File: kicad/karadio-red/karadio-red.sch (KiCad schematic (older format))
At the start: 18 parts, among them J1 CTRL, J2 PWR, J3 UART, J4 FW, J5 VS1053_RED, SW1 RESET, U1 AMS1117-3.3, U2 ESP-12E

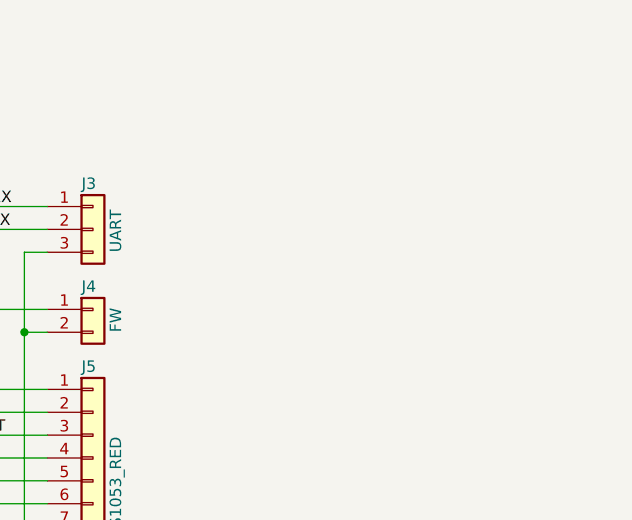
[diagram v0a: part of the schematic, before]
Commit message: Add optional RAM to karadio project
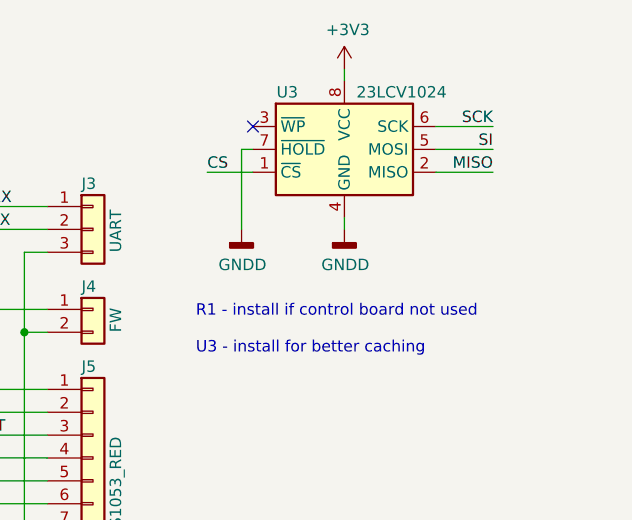
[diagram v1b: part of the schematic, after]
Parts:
- added U3: 23LCV1024, Package_SO:SO-8_3.9x4.9mm_P1.27mm, symbol Memory_EEPROM:25LCxxx
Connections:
- net +3V3: now also U3.8 (VCC)
- net CS: now also U3.1 (~CS)
- net GNDD: now also U3.4 (GND), U3.7 (~HOLD)
- net MISO: now also U3.2 (MISO)
- net SCK: now also U3.6 (SCK)
- net SI: now also U3.5 (MOSI)
- no-connect marks 6 -> 7
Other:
- note added: "R1 - install if control board not used\n\nU3 - install for better caching"
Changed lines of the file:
@@
 EESchema Schematic File Version 4
+LIBS:karadio-red-cache
 EELAYER 29 0
 EELAYER END
@@
 Text Label 4850 3300 0    50   ~ 0
 ~RST
+$Comp
+L Memory_EEPROM:25LCxxx U3
+U 1 1 5D361D11
+P 9000 3050
+F 0 "U3" H 8750 3300 50  0000 C CNN
+F 1 "23LCV1024" H 9250 3300 50  0000 C CNN
+F 2 "Package_SO:SO-8_3.9x4.9mm_P1.27mm" H 9000 3050 50  0001 C CNN
+F 3 "http://ww1.microchip.com/downloads/en/DeviceDoc/21832H.pdf" H 9000 3050 50  0001 C CNN
+	1    9000 3050
+	1    0    0    -1
+$EndComp
+$Comp
+L power:+3V3 #PWR0120
+U 1 1 5D3667F3
+P 9000 2700
+F 0 "#PWR0120" H 9000 2550 50  0001 C CNN
+F 1 "+3V3" H 9015 2873 50  0000 C CNN
+F 2 "" H 9000 2700 50  0001 C CNN
+F 3 "" H 9000 2700 50  0001 C CNN
+	1    9000 2700
+	1    0    0    -1
+$EndComp
+Wire Wire Line
+	9000 2700 9000 2750
+$Comp
+L power:GNDD #PWR0121
+U 1 1 5D369461
+P 9000 3400
+F 0 "#PWR0121" H 9000 3150 50  0001 C CNN
+F 1 "GNDD" H 9004 3245 50  0000 C CNN
+F 2 "" H 9000 3400 50  0001 C CNN
+F 3 "" H 9000 3400 50  0001 C CNN
+	1    9000 3400
+	1    0    0    -1
+$EndComp
+Wire Wire Line
+	9000 3400 9000 3350
+Text Label 8400 3150 0    50   ~ 0
+CS
+Wire Wire Line
+	8600 3150 8400 3150
+Text Label 9650 3150 2    50   ~ 0
+MISO
+Wire Wire Line
+	9650 3150 9400 3150
+NoConn ~ 8600 2950
+Wire Wire Line
+	9400 3050 9650 3050
+Text Label 9650 3050 2    50   ~ 0
+SI
+Wire Wire Line
+	9400 2950 9650 2950
+Text Label 9650 2950 2    50   ~ 0
+SCK
+$Comp
+L power:GNDD #PWR0122
+U 1 1 5D382FBD
+P 8550 3400
+F 0 "#PWR0122" H 8550 3150 50  0001 C CNN
+F 1 "GNDD" H 8554 3245 50  0000 C CNN
+F 2 "" H 8550 3400 50  0001 C CNN
+F 3 "" H 8550 3400 50  0001 C CNN
+	1    8550 3400
+	1    0    0    -1
+$EndComp
+Wire Wire Line
+	8600 3050 8550 3050
+Wire Wire Line
+	8550 3050 8550 3400
+Text Notes 8350 3950 0    50   ~ 0
+R1 - install if control board not used\n\nU3 - install for better caching
 $EndSCHEMATC

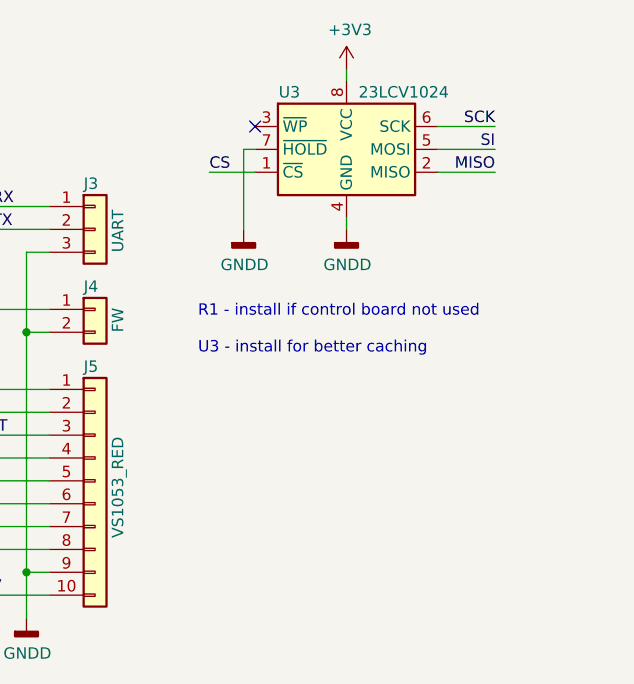
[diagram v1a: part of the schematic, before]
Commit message: Make karadio project able to work with both 23LCV1024 and 23LC1024
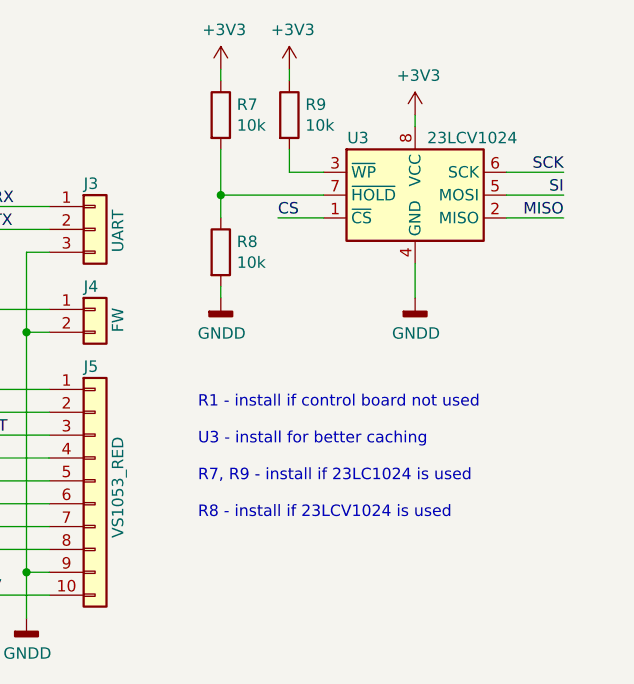
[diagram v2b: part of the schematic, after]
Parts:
- added R7, R8, R9: 10k, Resistor_SMD:R_1206_3216Metric, symbol Device:R
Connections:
- net +3V3: now also R7.1, R9.1
- net GNDD: now also R8.2; no longer U3.7 (~HOLD)
- net at U3.3 (~WP): now also R9.2
- new net: R7.2, R8.1, U3.7 (~HOLD)
- no-connect marks 7 -> 6
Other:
- note added: "R1 - install if control board not used\n\nU3 - install for better caching\n\nR7, R9 - install if 23LC1024 is used\n\nR8 - install if 23LCV1024 is used\n\n"
- note removed: "R1 - install if control board not used\n\nU3 - install for better caching"
- moved on the sheet: U3
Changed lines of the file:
@@
 L Memory_EEPROM:25LCxxx U3
 U 1 1 5D361D11
-P 9000 3050
-F 0 "U3" H 8750 3300 50  0000 C CNN
-F 1 "23LCV1024" H 9250 3300 50  0000 C CNN
-F 2 "Package_SO:SO-8_3.9x4.9mm_P1.27mm" H 9000 3050 50  0001 C CNN
-F 3 "http://ww1.microchip.com/downloads/en/DeviceDoc/21832H.pdf" H 9000 3050 50  0001 C CNN
-	1    9000 3050
+P 9300 3250
+F 0 "U3" H 9050 3500 50  0000 C CNN
+F 1 "23LCV1024" H 9550 3500 50  0000 C CNN
+F 2 "Package_SO:SO-8_3.9x4.9mm_P1.27mm" H 9300 3250 50  0001 C CNN
+F 3 "http://ww1.microchip.com/downloads/en/DeviceDoc/21832H.pdf" H 9300 3250 50  0001 C CNN
+	1    9300 3250
 	1    0    0    -1
 $EndComp
@@
 L power:+3V3 #PWR0120
 U 1 1 5D3667F3
-P 9000 2700
-F 0 "#PWR0120" H 9000 2550 50  0001 C CNN
-F 1 "+3V3" H 9015 2873 50  0000 C CNN
-F 2 "" H 9000 2700 50  0001 C CNN
-F 3 "" H 9000 2700 50  0001 C CNN
-	1    9000 2700
+P 9300 2900
+F 0 "#PWR0120" H 9300 2750 50  0001 C CNN
+F 1 "+3V3" H 9315 3073 50  0000 C CNN
+F 2 "" H 9300 2900 50  0001 C CNN
+F 3 "" H 9300 2900 50  0001 C CNN
+	1    9300 2900
 	1    0    0    -1
 $EndComp
 Wire Wire Line
-	9000 2700 9000 2750
+	9300 2900 9300 2950
 $Comp
 L power:GNDD #PWR0121
 U 1 1 5D369461
-P 9000 3400
-F 0 "#PWR0121" H 9000 3150 50  0001 C CNN
-F 1 "GNDD" H 9004 3245 50  0000 C CNN
-F 2 "" H 9000 3400 50  0001 C CNN
-F 3 "" H 9000 3400 50  0001 C CNN
-	1    9000 3400
+P 9300 3700
+F 0 "#PWR0121" H 9300 3450 50  0001 C CNN
+F 1 "GNDD" H 9304 3545 50  0000 C CNN
+F 2 "" H 9300 3700 50  0001 C CNN
+F 3 "" H 9300 3700 50  0001 C CNN
+	1    9300 3700
 	1    0    0    -1
 $EndComp
 Wire Wire Line
-	9000 3400 9000 3350
-Text Label 8400 3150 0    50   ~ 0
-CS
-Wire Wire Line
-	8600 3150 8400 3150
-Text Label 9650 3150 2    50   ~ 0
+	9300 3700 9300 3550
+Text Label 9950 3350 2    50   ~ 0
 MISO
 Wire Wire Line
-	9650 3150 9400 3150
-NoConn ~ 8600 2950
+	9950 3350 9700 3350
 Wire Wire Line
-	9400 3050 9650 3050
-Text Label 9650 3050 2    50   ~ 0
+	9700 3250 9950 3250
+Text Label 9950 3250 2    50   ~ 0
 SI
 Wire Wire Line
-	9400 2950 9650 2950
-Text Label 9650 2950 2    50   ~ 0
+	9700 3150 9950 3150
+Text Label 9950 3150 2    50   ~ 0
 SCK
 $Comp
 L power:GNDD #PWR0122
 U 1 1 5D382FBD
-P 8550 3400
-F 0 "#PWR0122" H 8550 3150 50  0001 C CNN
-F 1 "GNDD" H 8554 3245 50  0000 C CNN
-F 2 "" H 8550 3400 50  0001 C CNN
-F 3 "" H 8550 3400 50  0001 C CNN
-	1    8550 3400
+P 8450 3700
+F 0 "#PWR0122" H 8450 3450 50  0001 C CNN
+F 1 "GNDD" H 8454 3545 50  0000 C CNN
+F 2 "" H 8450 3700 50  0001 C CNN
+F 3 "" H 8450 3700 50  0001 C CNN
+	1    8450 3700
+	1    0    0    -1
+$EndComp
+Text Notes 8350 4750 0    50   ~ 0
+R1 - install if control board not used\n\nU3 - install for better caching\n\nR7, R9 - install if 23LC1024 is used\n\nR8 - install if 23LCV1024 is used\n\n
+Wire Wire Line
+	8450 3050 8450 3250
+$Comp
+L Device:R R8
+U 1 1 5D387CD5
+P 8450 3500
+F 0 "R8" H 8520 3546 50  0000 L CNN
+F 1 "10k" H 8520 3455 50  0000 L CNN
+F 2 "Resistor_SMD:R_1206_3216Metric" V 8380 3500 50  0001 C CNN
+F 3 "~" H 8450 3500 50  0001 C CNN
+	1    8450 3500
+	1    0    0    -1
+$EndComp
+$Comp
+L Device:R R7
+U 1 1 5D3871DC
+P 8450 2900
+F 0 "R7" H 8520 2946 50  0000 L CNN
+F 1 "10k" H 8520 2855 50  0000 L CNN
+F 2 "Resistor_SMD:R_1206_3216Metric" V 8380 2900 50  0001 C CNN
+F 3 "~" H 8450 2900 50  0001 C CNN
+	1    8450 2900
 	1    0    0    -1
 $EndComp
 Wire Wire Line
-	8600 3050 8550 3050
+	8900 3350 8700 3350
+Text Label 8700 3350 0    50   ~ 0
+CS
 Wire Wire Line
-	8550 3050 8550 3400
-Text Notes 8350 3950 0    50   ~ 0
-R1 - install if control board not used\n\nU3 - install for better caching
+	8450 3250 8900 3250
+Connection ~ 8450 3250
+Wire Wire Line
+	8450 3250 8450 3350
+$Comp
+L power:+3V3 #PWR02
+U 1 1 5D399E65
+P 8450 2700
+F 0 "#PWR02" H 8450 2550 50  0001 C CNN
+F 1 "+3V3" H 8465 2873 50  0000 C CNN
+F 2 "" H 8450 2700 50  0001 C CNN
+F 3 "" H 8450 2700 50  0001 C CNN
+	1    8450 2700
+	1    0    0    -1
+$EndComp
+Wire Wire Line
+	8450 2700 8450 2750
+$Comp
+L Device:R R9
+U 1 1 5D3A2230
+P 8750 2900
+F 0 "R9" H 8820 2946 50  0000 L CNN
+F 1 "10k" H 8820 2855 50  0000 L CNN
+F 2 "Resistor_SMD:R_1206_3216Metric" V 8680 2900 50  0001 C CNN
+F 3 "~" H 8750 2900 50  0001 C CNN
+	1    8750 2900
+	1    0    0    -1
+$EndComp
+$Comp
+L power:+3V3 #PWR03
+U 1 1 5D3A389D
+P 8750 2700
+F 0 "#PWR03" H 8750 2550 50  0001 C CNN
+F 1 "+3V3" H 8765 2873 50  0000 C CNN
+F 2 "" H 8750 2700 50  0001 C CNN
+F 3 "" H 8750 2700 50  0001 C CNN
+	1    8750 2700
+	1    0    0    -1
+$EndComp
+Wire Wire Line
+	8750 2700 8750 2750
+Wire Wire Line
+	8750 3050 8750 3150
+Wire Wire Line
+	8750 3150 8900 3150
+Wire Wire Line
+	8450 3650 8450 3700
 $EndSCHEMATC
